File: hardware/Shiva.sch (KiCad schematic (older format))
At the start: 69 parts, among them J1 JACK_FEMALE_STEREO, J2 JACK_FEMALE_STEREO, J3 JACK_FEMALE_STEREO, J4 JACK_FEMALE_STEREO, J5 JACK_FEMALE_STEREO, J6 JACK_FEMALE_STEREO, J7 JACK_FEMALE_STEREO, J8 JACK_FEMALE_STEREO, P1 DIN_5, U1 LTC6242, U2 LTC6242, U3 LD1117S33CTR

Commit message: Fix SMD footprints too small
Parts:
- D1, D10, D11, D12, D13, D14, D15, D16, D2, D3, D4, D5, D6, D7, D8, D9: footprint Diodes_SMD:SOD-323 -> Diodes_SMD:D_SOD-323_HandSoldering
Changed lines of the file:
@@
 F 0 "D7" H 3400 1450 50  0000 C CNN
 F 1 "3.3V" H 3400 1250 50  0000 C CNN
-F 2 "Diodes_SMD:SOD-323" H 3400 1350 60  0001 C CNN
+F 2 "Diodes_SMD:D_SOD-323_HandSoldering" H 3400 1350 60  0001 C CNN
 F 3 "" H 3400 1350 60  0000 C CNN
 	1    3400 1350
@@
 F 0 "D8" H 3400 1950 50  0000 C CNN
 F 1 "3.3V" H 3400 1750 50  0000 C CNN
-F 2 "Diodes_SMD:SOD-323" H 3400 1850 60  0001 C CNN
+F 2 "Diodes_SMD:D_SOD-323_HandSoldering" H 3400 1850 60  0001 C CNN
 F 3 "" H 3400 1850 60  0000 C CNN
 	1    3400 1850
@@
 F 0 "D3" H 3350 3500 50  0000 C CNN
 F 1 "3.3V" H 3350 3300 50  0000 C CNN
-F 2 "Diodes_SMD:SOD-323" H 3350 3400 60  0001 C CNN
+F 2 "Diodes_SMD:D_SOD-323_HandSoldering" H 3350 3400 60  0001 C CNN
 F 3 "" H 3350 3400 60  0000 C CNN
 	1    3350 3400
@@
 F 0 "D4" H 3350 4000 50  0000 C CNN
 F 1 "3.3V" H 3350 3800 50  0000 C CNN
-F 2 "Diodes_SMD:SOD-323" H 3350 3900 60  0001 C CNN
+F 2 "Diodes_SMD:D_SOD-323_HandSoldering" H 3350 3900 60  0001 C CNN
 F 3 "" H 3350 3900 60  0000 C CNN
 	1    3350 3900
@@
 F 0 "D5" H 3350 5600 50  0000 C CNN
 F 1 "3.3V" H 3350 5400 50  0000 C CNN
-F 2 "Diodes_SMD:SOD-323" H 3350 5500 60  0001 C CNN
+F 2 "Diodes_SMD:D_SOD-323_HandSoldering" H 3350 5500 60  0001 C CNN
 F 3 "" H 3350 5500 60  0000 C CNN
 	1    3350 5500
@@
 F 0 "D6" H 3350 6100 50  0000 C CNN
 F 1 "3.3V" H 3350 5900 50  0000 C CNN
-F 2 "Diodes_SMD:SOD-323" H 3350 6000 60  0001 C CNN
+F 2 "Diodes_SMD:D_SOD-323_HandSoldering" H 3350 6000 60  0001 C CNN
 F 3 "" H 3350 6000 60  0000 C CNN
 	1    3350 6000
@@
 F 0 "D1" H 3300 7650 50  0000 C CNN
 F 1 "3.3V" H 3300 7450 50  0000 C CNN
-F 2 "Diodes_SMD:SOD-323" H 3300 7550 60  0001 C CNN
+F 2 "Diodes_SMD:D_SOD-323_HandSoldering" H 3300 7550 60  0001 C CNN
 F 3 "" H 3300 7550 60  0000 C CNN
 	1    3300 7550
@@
 F 0 "D2" H 3300 8150 50  0000 C CNN
 F 1 "3.3V" H 3300 7950 50  0000 C CNN
-F 2 "Diodes_SMD:SOD-323" H 3300 8050 60  0001 C CNN
+F 2 "Diodes_SMD:D_SOD-323_HandSoldering" H 3300 8050 60  0001 C CNN
 F 3 "" H 3300 8050 60  0000 C CNN
 	1    3300 8050
@@
 F 0 "D15" H 8500 1400 50  0000 C CNN
 F 1 "3.3V" H 8500 1200 50  0000 C CNN
-F 2 "Diodes_SMD:SOD-323" H 8500 1300 60  0001 C CNN
+F 2 "Diodes_SMD:D_SOD-323_HandSoldering" H 8500 1300 60  0001 C CNN
 F 3 "" H 8500 1300 60  0000 C CNN
 	1    8500 1300
@@
 F 0 "D16" H 8500 1900 50  0000 C CNN
 F 1 "3.3V" H 8500 1700 50  0000 C CNN
-F 2 "Diodes_SMD:SOD-323" H 8500 1800 60  0001 C CNN
+F 2 "Diodes_SMD:D_SOD-323_HandSoldering" H 8500 1800 60  0001 C CNN
 F 3 "" H 8500 1800 60  0000 C CNN
 	1    8500 1800
@@
 F 0 "D11" H 8450 3450 50  0000 C CNN
 F 1 "3.3V" H 8450 3250 50  0000 C CNN
-F 2 "Diodes_SMD:SOD-323" H 8450 3350 60  0001 C CNN
+F 2 "Diodes_SMD:D_SOD-323_HandSoldering" H 8450 3350 60  0001 C CNN
 F 3 "" H 8450 3350 60  0000 C CNN
 	1    8450 3350
@@
 F 0 "D12" H 8450 3950 50  0000 C CNN
 F 1 "3.3V" H 8450 3750 50  0000 C CNN
-F 2 "Diodes_SMD:SOD-323" H 8450 3850 60  0001 C CNN
+F 2 "Diodes_SMD:D_SOD-323_HandSoldering" H 8450 3850 60  0001 C CNN
 F 3 "" H 8450 3850 60  0000 C CNN
 	1    8450 3850
@@
 F 0 "D13" H 8450 5550 50  0000 C CNN
 F 1 "3.3V" H 8450 5350 50  0000 C CNN
-F 2 "Diodes_SMD:SOD-323" H 8450 5450 60  0001 C CNN
+F 2 "Diodes_SMD:D_SOD-323_HandSoldering" H 8450 5450 60  0001 C CNN
 F 3 "" H 8450 5450 60  0000 C CNN
 	1    8450 5450
@@
 F 0 "D14" H 8450 6050 50  0000 C CNN
 F 1 "3.3V" H 8450 5850 50  0000 C CNN
-F 2 "Diodes_SMD:SOD-323" H 8450 5950 60  0001 C CNN
+F 2 "Diodes_SMD:D_SOD-323_HandSoldering" H 8450 5950 60  0001 C CNN
 F 3 "" H 8450 5950 60  0000 C CNN
 	1    8450 5950
@@
 F 0 "D9" H 8400 7600 50  0000 C CNN
 F 1 "3.3V" H 8400 7400 50  0000 C CNN
-F 2 "Diodes_SMD:SOD-323" H 8400 7500 60  0001 C CNN
+F 2 "Diodes_SMD:D_SOD-323_HandSoldering" H 8400 7500 60  0001 C CNN
 F 3 "" H 8400 7500 60  0000 C CNN
 	1    8400 7500
@@
 F 0 "D10" H 8400 8100 50  0000 C CNN
 F 1 "3.3V" H 8400 7900 50  0000 C CNN
-F 2 "Diodes_SMD:SOD-323" H 8400 8000 60  0001 C CNN
+F 2 "Diodes_SMD:D_SOD-323_HandSoldering" H 8400 8000 60  0001 C CNN
 F 3 "" H 8400 8000 60  0000 C CNN
 	1    8400 8000

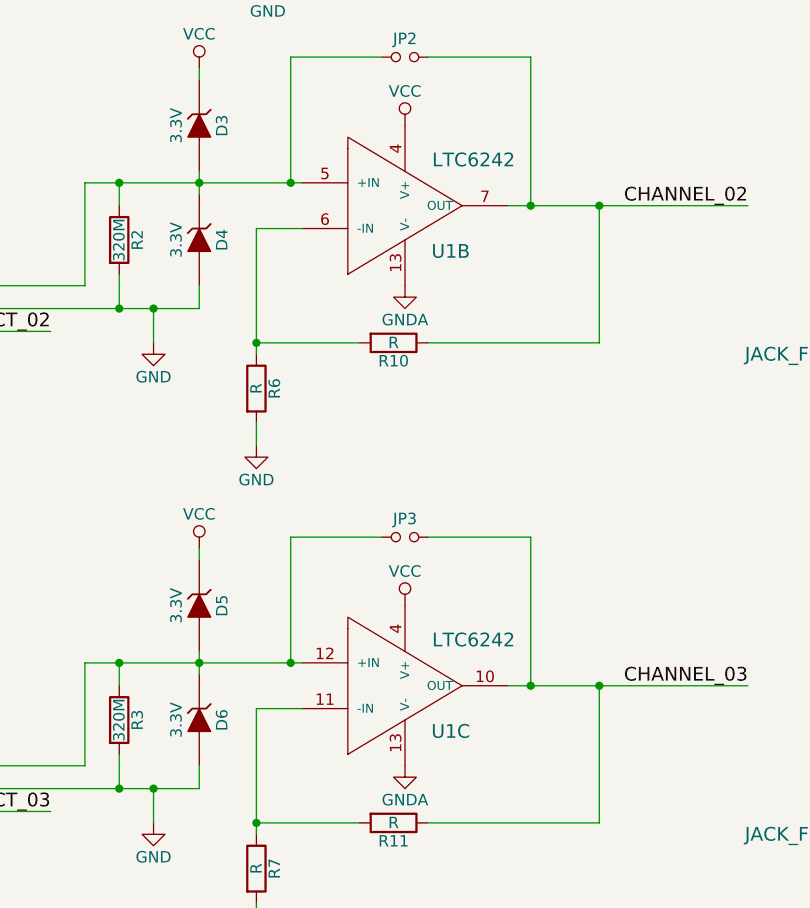
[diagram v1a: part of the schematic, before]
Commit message: Route channel 3
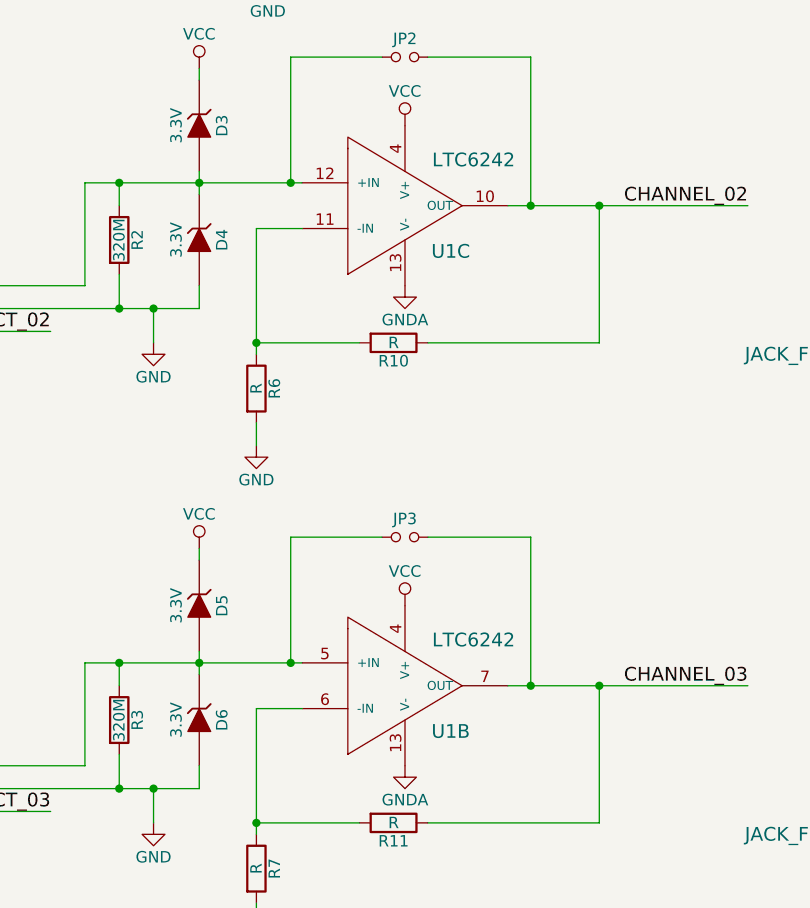
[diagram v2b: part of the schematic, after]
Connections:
- net CHANNEL_02: now also U1.10 (OUT); no longer U1.7 (OUT)
- net CHANNEL_03: now also U1.7 (OUT); no longer U1.10 (OUT)
- net at D3.2 (A), D4.1 (K), J2.T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: now also U1.12 (+IN); no longer U1.5 (+IN)
- net at R10.2, R6.1: now also U1.11 (-IN); no longer U1.6 (-IN)
- net at D5.2 (A), D6.1 (K), J3.T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: now also U1.5 (+IN); no longer U1.12 (+IN)
- net at R11.2, R7.1: now also U1.6 (-IN); no longer U1.11 (-IN)
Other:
- moved on the sheet: U1B, U1C
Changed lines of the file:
@@
 L ANALOG_LTC6242 U1
 U 2 1 56242AD4
-P 4200 3900
-F 0 "U1" H 4450 3850 60  0000 C CNN
-F 1 "LTC6242" H 4550 4250 60  0000 C CNN
-F 2 "def-footprints:Package_SSOP16" H 4200 3900 60  0001 C CNN
-F 3 "" H 4200 3900 60  0000 C CNN
-	2    4200 3900
+P 4200 6000
+F 0 "U1" H 4450 5950 60  0000 C CNN
+F 1 "LTC6242" H 4550 6350 60  0000 C CNN
+F 2 "def-footprints:Package_SSOP16" H 4200 6000 60  0001 C CNN
+F 3 "" H 4200 6000 60  0000 C CNN
+	2    4200 6000
 	1    0    0    -1
 $EndComp
@@
 L ANALOG_LTC6242 U1
 U 3 1 56244F0F
-P 4200 6000
-F 0 "U1" H 4450 5950 60  0000 C CNN
-F 1 "LTC6242" H 4550 6350 60  0000 C CNN
-F 2 "def-footprints:Package_SSOP16" H 4200 6000 60  0001 C CNN
-F 3 "" H 4200 6000 60  0000 C CNN
-	3    4200 6000
+P 4200 3900
+F 0 "U1" H 4450 3850 60  0000 C CNN
+F 1 "LTC6242" H 4550 4250 60  0000 C CNN
+F 2 "def-footprints:Package_SSOP16" H 4200 3900 60  0001 C CNN
+F 3 "" H 4200 3900 60  0000 C CNN
+	3    4200 3900
 	1    0    0    -1
 $EndComp

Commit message: Document channel swap in schematic
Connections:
- net CHANNEL_02: now also BOARD1.20 (Touch/SDA0/A4/D18); no longer BOARD1.19 (Touch/SDA0/A3/D17)
- net CHANNEL_03: now also BOARD1.19 (Touch/SDA0/A3/D17); no longer BOARD1.20 (Touch/SDA0/A4/D18)
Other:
- note added: "(Swapping these channels \nsimplifies routing)"
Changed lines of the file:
@@
 Wire Wire Line
 	14950 2150 15600 2150
+Text Label 15600 2350 2    60   ~ 0
+CHANNEL_03
+Wire Wire Line
+	14950 2250 15600 2250
 Text Label 15600 2250 2    60   ~ 0
-CHANNEL_03
-Wire Wire Line
-	14950 2250 15600 2250
-Text Label 15600 2350 2    60   ~ 0
 CHANNEL_02
 Wire Wire Line
@@
 Wire Wire Line
 	3350 3200 3350 3150
+Text Notes 14800 3250 0    60   ~ 0
+(Swapping these channels \nsimplifies routing)
+Wire Notes Line
+	15850 2200 15850 3050
+Wire Notes Line
+	15850 2300 15650 2300
+Wire Notes Line
+	15650 2200 15850 2200
 $EndSCHEMATC

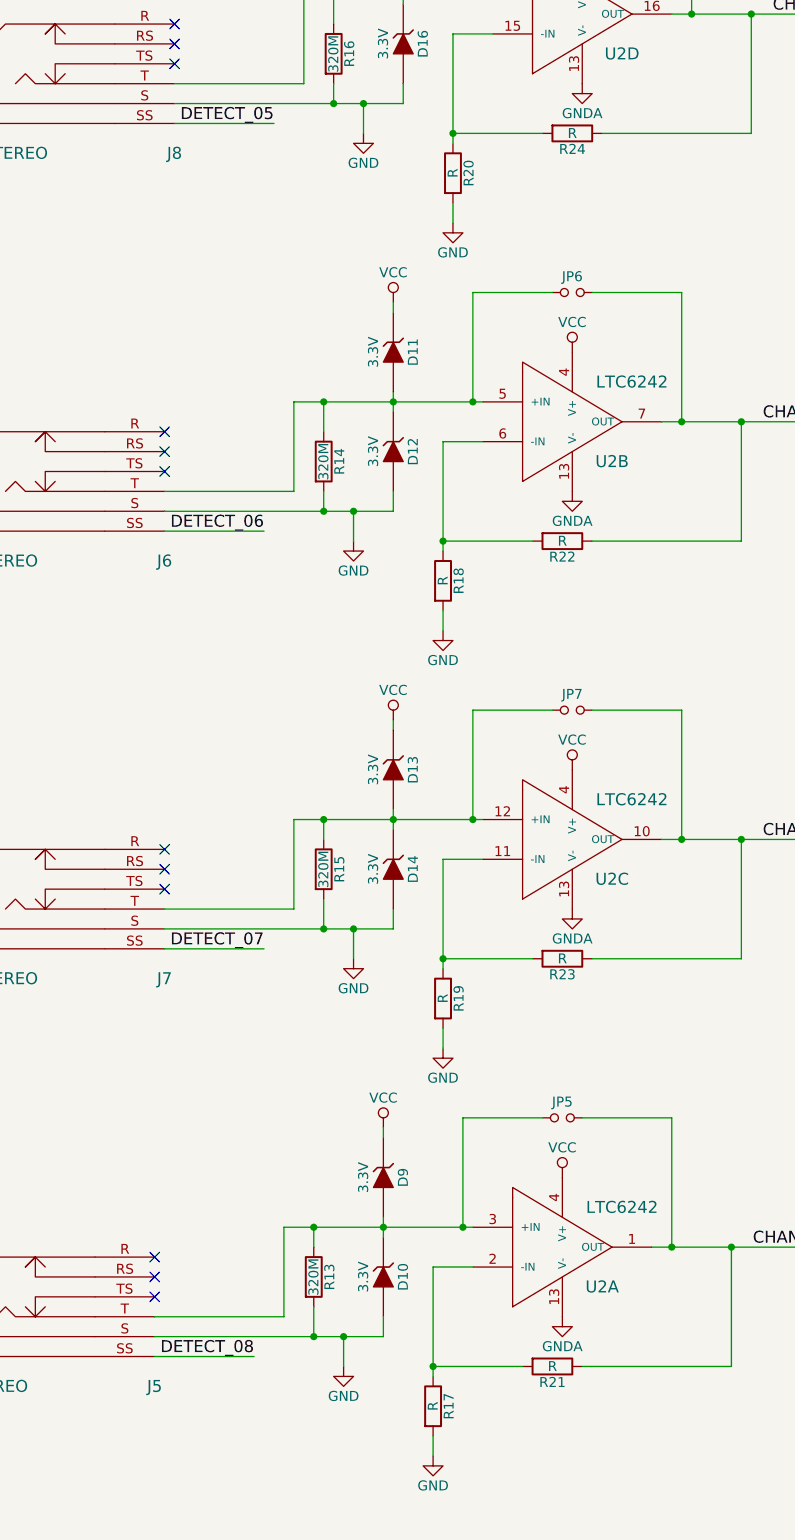
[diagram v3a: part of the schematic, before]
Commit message: Route channel 5, swap channels to simplify op-amp routing
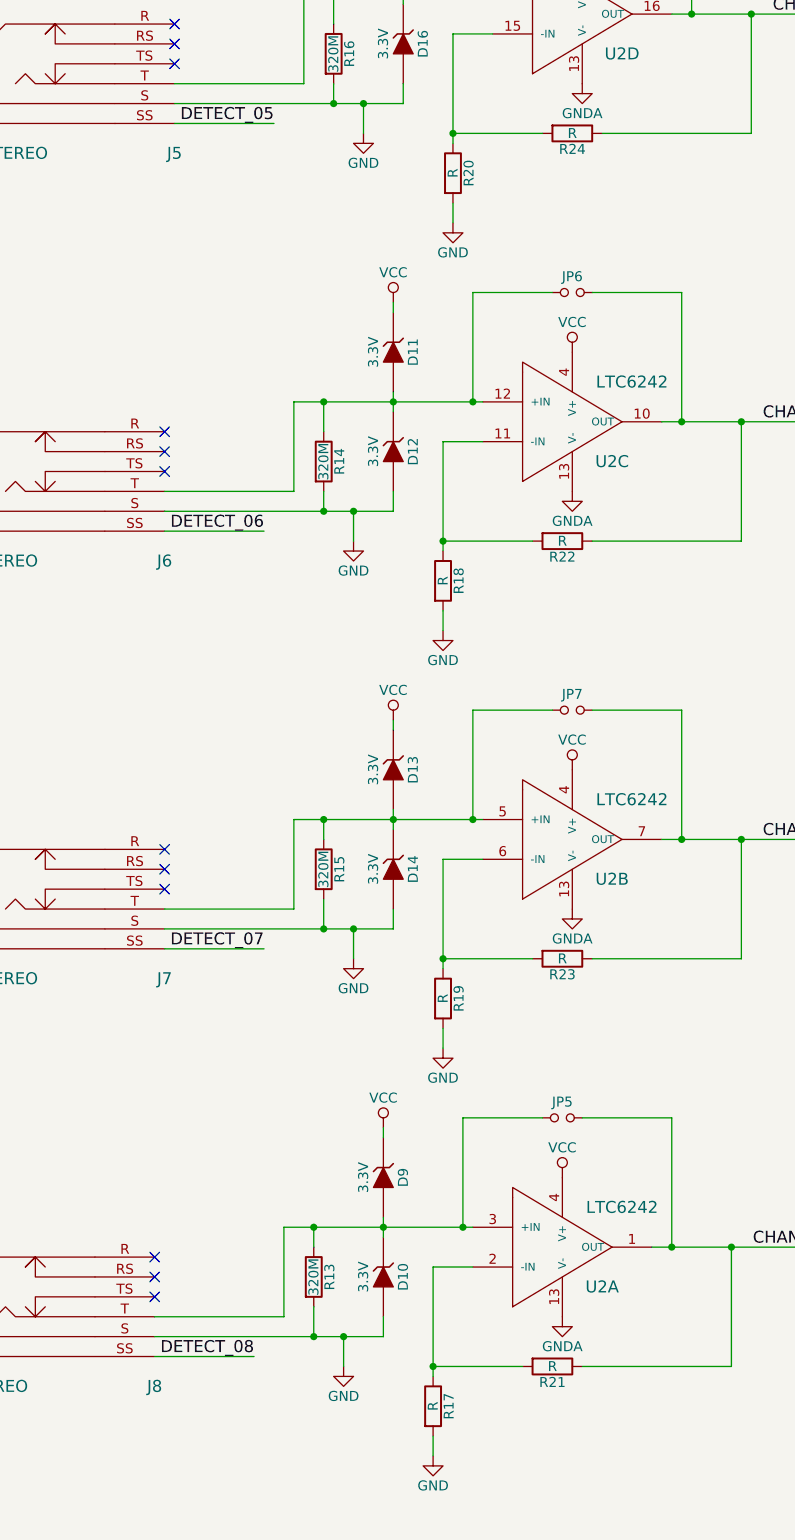
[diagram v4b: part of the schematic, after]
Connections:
- net CHANNEL_06: now also U2.10 (OUT); no longer U2.7 (OUT)
- net CHANNEL_07: now also U2.7 (OUT); no longer U2.10 (OUT)
- net DETECT_05: now also J5.SS; no longer J8.SS
- net DETECT_08: now also J8.SS; no longer J5.SS
- net at D15.2 (A), D16.1 (K), JP8.1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: now also J5.T; no longer J8.T
- net at D11.2 (A), D12.1 (K), J6.T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: now also U2.12 (+IN); no longer U2.5 (+IN)
- net at R18.1, R22.2: now also U2.11 (-IN); no longer U2.6 (-IN)
- net at D13.2 (A), D14.1 (K), J7.T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: now also U2.5 (+IN); no longer U2.12 (+IN)
- net at R19.1, R23.2: now also U2.6 (-IN); no longer U2.11 (-IN)
- net at D10.1 (K), D9.2 (A), JP5.1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: now also J8.T; no longer J5.T
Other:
- moved on the sheet: J5, J8, U2B, U2C
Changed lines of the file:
@@
 L CONNECTORS_JACK_FEMALE_STEREO_6_PINS J8
 U 1 1 562466BF
-P 6800 1850
-F 0 "J8" H 7350 1350 60  0000 C CNN
-F 1 "JACK_FEMALE_STEREO" H 6250 1350 60  0000 C CNN
-F 2 "def-footprints:CONN_Jack_Female_6.35mm_THD" H 7250 1800 60  0001 C CNN
-F 3 "" H 7250 1800 60  0000 C CNN
-	1    6800 1850
+P 6700 8050
+F 0 "J8" H 7250 7550 60  0000 C CNN
+F 1 "JACK_FEMALE_STEREO" H 6150 7550 60  0000 C CNN
+F 2 "def-footprints:CONN_Jack_Female_6.35mm_THD" H 7150 8000 60  0001 C CNN
+F 3 "" H 7150 8000 60  0000 C CNN
+	1    6700 8050
 	1    0    0    -1
 $EndComp
@@
 L ANALOG_LTC6242 U2
 U 2 1 56246786
-P 9300 3850
-F 0 "U2" H 9550 3800 60  0000 C CNN
-F 1 "LTC6242" H 9650 4200 60  0000 C CNN
-F 2 "def-footprints:Package_SSOP16" H 9300 3850 60  0001 C CNN
-F 3 "" H 9300 3850 60  0000 C CNN
-	2    9300 3850
+P 9300 5950
+F 0 "U2" H 9550 5900 60  0000 C CNN
+F 1 "LTC6242" H 9650 6300 60  0000 C CNN
+F 2 "def-footprints:Package_SSOP16" H 9300 5950 60  0001 C CNN
+F 3 "" H 9300 5950 60  0000 C CNN
+	2    9300 5950
 	1    0    0    -1
 $EndComp
@@
 L ANALOG_LTC6242 U2
 U 3 1 562467F3
-P 9300 5950
-F 0 "U2" H 9550 5900 60  0000 C CNN
-F 1 "LTC6242" H 9650 6300 60  0000 C CNN
-F 2 "def-footprints:Package_SSOP16" H 9300 5950 60  0001 C CNN
-F 3 "" H 9300 5950 60  0000 C CNN
-	3    9300 5950
+P 9300 3850
+F 0 "U2" H 9550 3800 60  0000 C CNN
+F 1 "LTC6242" H 9650 4200 60  0000 C CNN
+F 2 "def-footprints:Package_SSOP16" H 9300 3850 60  0001 C CNN
+F 3 "" H 9300 3850 60  0000 C CNN
+	3    9300 3850
 	1    0    0    -1
 $EndComp
@@
 L CONNECTORS_JACK_FEMALE_STEREO_6_PINS J5
 U 1 1 56246806
-P 6700 8050
-F 0 "J5" H 7250 7550 60  0000 C CNN
-F 1 "JACK_FEMALE_STEREO" H 6150 7550 60  0000 C CNN
-F 2 "def-footprints:CONN_Jack_Female_6.35mm_THD" H 7150 8000 60  0001 C CNN
-F 3 "" H 7150 8000 60  0000 C CNN
-	1    6700 8050
-	1    0    0    -1
-$EndComp
+P 6800 1850
+F 0 "J5" H 7350 1350 60  0000 C CNN
+F 1 "JACK_FEMALE_STEREO" H 6250 1350 60  0000 C CNN
+F 2 "def-footprints:CONN_Jack_Female_6.35mm_THD" H 7250 1800 60  0001 C CNN
+F 3 "" H 7250 1800 60  0000 C CNN
+	1    6800 1850
+	1    0    0    -1
+$EndComp

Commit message: Add more LEDs to schematic
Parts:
- added D? (x8): LED, symbol LED
- added Q? (x8): Q_NMOS_DGS, symbol Q_NMOS_DGS
- added R? (x8): 4K7, Resistors_SMD:R_0603_HandSoldering, symbol R
- added R? (x8): 100R, Resistors_SMD:R_0603_HandSoldering, symbol R
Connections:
- net DETECT_01: now also R?.2, R?.2, R?.2, R?.2, R?.2, R?.2, R?.2, R?.2; no longer J4.SS
- net GND: now also Q?.3 (S), Q?.3 (S), Q?.3 (S), Q?.3 (S), Q?.3 (S), Q?.3 (S), Q?.3 (S), Q?.3 (S)
- net VCC: now also D?.2 (A), D?.2 (A), D?.2 (A), D?.2 (A), D?.2 (A), D?.2 (A), D?.2 (A), D?.2 (A)
- new net: D?.1 (K), R?.1 (x8)
- new net: Q?.1 (D), R?.2 (x8)
- new net CHANNEL_01_SW: J4.SS, Q?.2 (G), Q?.2 (G), Q?.2 (G), Q?.2 (G), Q?.2 (G), Q?.2 (G), Q?.2 (G), Q?.2 (G), R?.1, R?.1, R?.1, R?.1, R?.1, R?.1, R?.1, R?.1
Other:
- moved on the sheet: C3, C4, JP10, JP9, P1, R25, R26, U3
